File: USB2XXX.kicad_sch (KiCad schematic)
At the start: 16 parts, among them J1 Conn_01x04, J2 Conn_01x03, J3 Conn_01x02, J4 Conn_01x02, J5 Conn_01x02

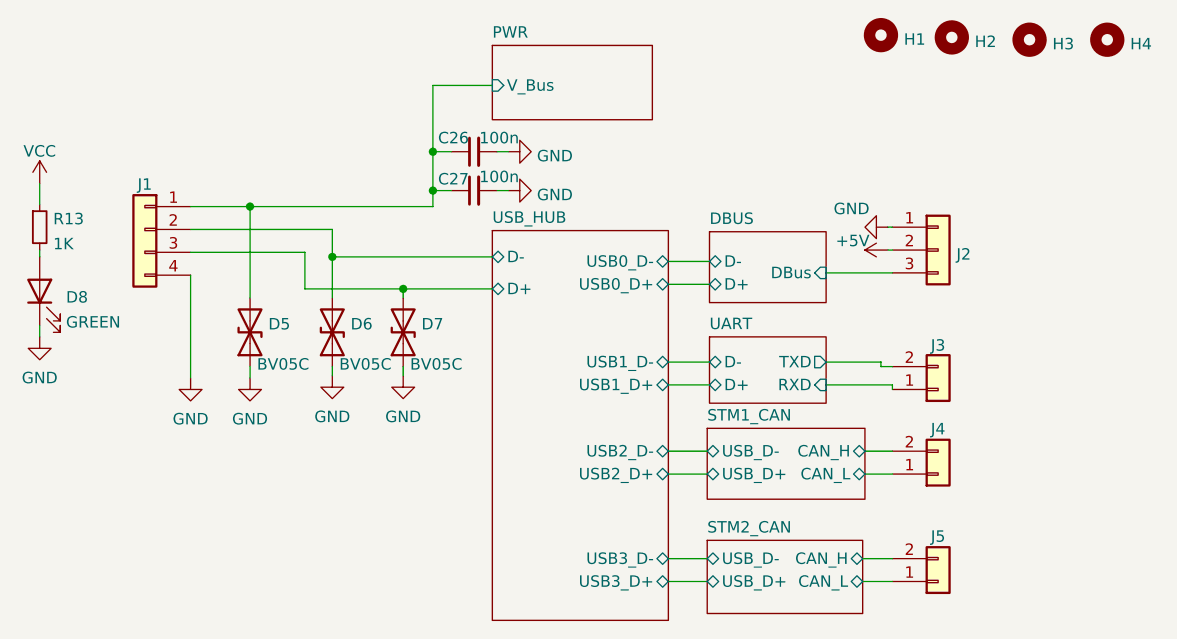
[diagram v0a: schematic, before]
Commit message: Change connectors back to GH1.25&Add ESD for UART and CAN
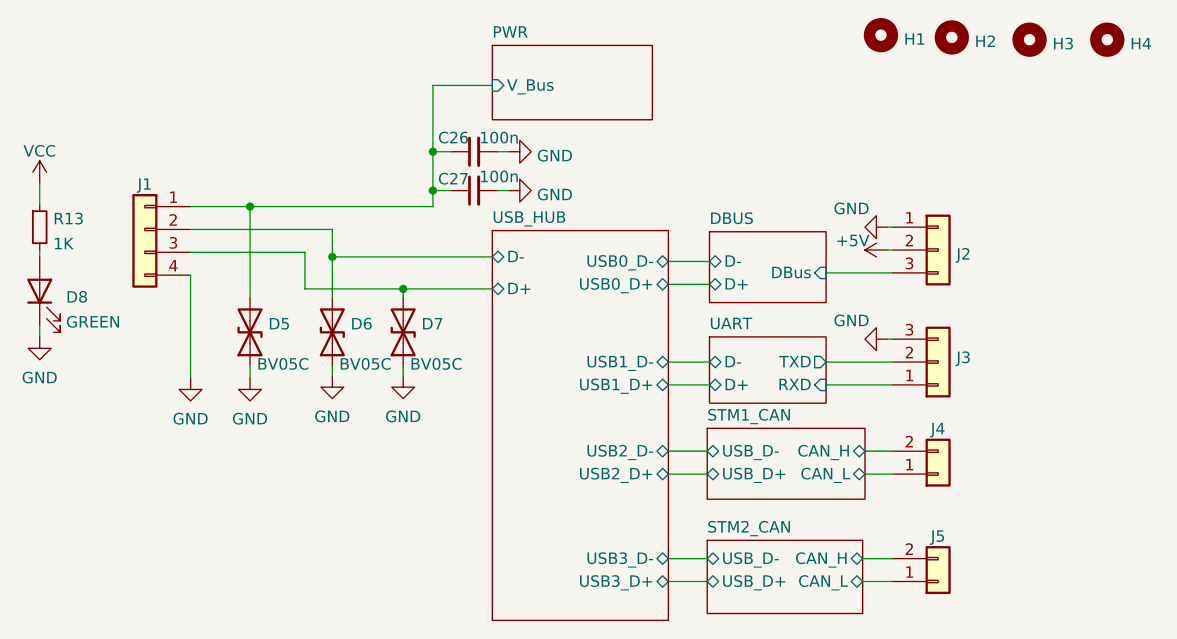
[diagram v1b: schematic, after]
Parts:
- removed J3: Conn_01x02, Connector:MountingHole_0.8mm_sm2.5_2pin, symbol Connector_Generic:Conn_01x02
- added J3: Conn_01x03, Connector_JST:JST_GH_SM03B-GHS-TB_1x03-1MP_P1.25mm_Horizontal, symbol Connector_Generic:Conn_01x03
- J4, J5: footprint Connector:MountingHole_0.8mm_sm2.5_2pin -> Connector_JST:JST_GH_SM02B-GHS-TB_1x02-1MP_P1.25mm_Horizontal
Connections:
- net GND: now also J3.3 (Pin_3)
- net UART/RXD: now also J3.1 (Pin_1)
- net UART/TXD: now also J3.2 (Pin_2)
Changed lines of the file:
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@@
     (stroke (width 0) (type default))
   )
-  (wire (pts (xy 167.64 100.33) (xy 166.37 100.33))
-    (stroke (width 0) (type default))
-  )
-  (wire (pts (xy 166.37 99.822) (xy 160.274 99.822))
+  (wire (pts (xy 160.274 99.822) (xy 167.64 99.822))
     (stroke (width 0) (type default))
   )
@@
     (stroke (width 0) (type default))
   )
+  (wire (pts (xy 167.132 97.282) (xy 167.64 97.282))
+    (stroke (width 0) (type default))
+  )
   (wire (pts (xy 116.586 69.088) (xy 116.586 76.454))
     (stroke (width 0) (type default))
@@
   )
   (wire (pts (xy 72.898 87.376) (xy 72.898 88.138))
-    (stroke (width 0) (type default))
-  )
-  (wire (pts (xy 167.64 102.87) (xy 167.64 102.362))
-    (stroke (width 0) (type default))
-  )
-  (wire (pts (xy 166.37 100.33) (xy 166.37 99.822))
     (stroke (width 0) (type default))
   )
@@
     )
   )
-  (symbol (lib_id "Connector_Generic:Conn_01x02") (at 172.72 102.87 0) (mirror x) (unit 1)
+  (symbol (lib_id "power:GND") (at 167.132 97.282 270) (unit 1)
     (in_bom yes) (on_board yes) (dnp no)
-    (property "Reference" "J3" (at 172.72 97.9711 0)
-      (effects (font (size 1.27 1.27)))
-    )
-    (property "Value" "Conn_01x02" (at 174.752 101.0034 0)
+    (property "Reference" "#PWR087" (at 160.782 97.282 0)
+      (effects (font (size 1.27 1.27)) hide)
+    )
+    (property "Value" "GND" (at 165.1 95.25 90)
+      (effects (font (size 1.27 1.27)) (justify right))
+    )
+    (property "Footprint" "" (at 167.132 97.282 0)
+      (effects (font (size 1.27 1.27)) hide)
+    )
+    (property "Datasheet" "" (at 167.132 97.282 0)
+      (effects (font (size 1.27 1.27)) hide)
+    )
+    (pin "1")
+    (instances
+      (project "USB2XXX"
+        (path "/e63e39d7-6ac0-4ffd-8aa3-1841a4541b55"
+          (reference "#PWR087") (unit 1)
+        )
+      )
+    )
+  )
+  (symbol (lib_id "Connector_Generic:Conn_01x03") (at 172.72 99.822 0) (mirror x) (unit 1)
+    (in_bom yes) (on_board yes) (dnp no)
+    (property "Reference" "J3" (at 174.752 99.343 0)
+      (effects (font (size 1.27 1.27)) (justify left))
+    )
+    (property "Value" "Conn_01x03" (at 174.752 97.9554 0)
       (effects (font (size 1.27 1.27)) (justify left) hide)
     )
-    (property "Footprint" "Connector:MountingHole_0.8mm_sm2.5_2pin" (at 172.72 102.87 0)
-      (effects (font (size 1.27 1.27)) hide)
-    )
-    (property "Datasheet" "~" (at 172.72 102.87 0)
-      (effects (font (size 1.27 1.27)) hide)
-    )
-    (pin "1")
-    (pin "2")
+    (property "Footprint" "Connector_JST:JST_GH_SM03B-GHS-TB_1x03-1MP_P1.25mm_Horizontal" (at 172.72 99.822 0)
+      (effects (font (size 1.27 1.27)) hide)
+    )
+    (property "Datasheet" "~" (at 172.72 99.822 0)
+      (effects (font (size 1.27 1.27)) hide)
+    )
+    (pin "1")
+    (pin "2")
+    (pin "3")
     (instances
       (project "USB2XXX"
@@
       (effects (font (size 1.27 1.27)) (justify left) hide)
     )
-    (property "Footprint" "Connector:MountingHole_0.8mm_sm2.5_2pin" (at 172.72 124.206 0)
+    (property "Footprint" "Connector_JST:JST_GH_SM02B-GHS-TB_1x02-1MP_P1.25mm_Horizontal" (at 172.72 124.206 0)
       (effects (font (size 1.27 1.27)) hide)
     )
@@
       (effects (font (size 1.27 1.27)) (justify left) hide)
     )
-    (property "Footprint" "Connector:MountingHole_0.8mm_sm2.5_2pin" (at 172.72 112.268 0)
-      (effects (font (size 1.27 1.27)) hide)
-    )
+    (property "Footprint" "Connector_JST:JST_GH_SM02B-GHS-TB_1x02-1MP_P1.25mm_Horizontal" (at 172.72 112.268 0)
+      (effects (font (size 1.27 1.27)) hide)
+    )
